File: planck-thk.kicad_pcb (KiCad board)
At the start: 2 copper layers, 228 x 114 mm, 134 parts, among them J2 Conn_01x05, J3 Qwiic, J4 Qwiic, J5 Qwiic, J6 JTAG, J7 ISP, J8 Reset, K1 Switch, K10 Switch, K11 Switch, K12 Switch, K13 Switch, K14 Switch, K15 Switch, K16 Switch, K17 Switch, K18 Switch, K19 Switch, K2 Switch, K20 Switch, K21 Switch, K22 Switch, K23 Switch, K24 Switch, K25 Switch, K26 Switch, K27 Switch, K28 Switch, K29 Switch, K3 Switch, K30 Switch, K31 Switch, K32 Switch, K33 Switch, K34 Switch, K35 Switch, K36 Switch, K37 Switch, K38 Switch, K39 Switch, K4 Switch, K40 Switch, K41 Switch, K42 Switch, K43 Switch, K44 Switch, K45 Switch, K46 Switch, K47 Switch, K48 Switch, K49 Switch, K5 Switch, K6 Switch, K7 Switch, K8 Switch, K9 Switch, SW1 SW_DIP_x04, SW2 Rotary_Encoder, SW3 Rotary_Encoder, U1 ATMEGA32A-PU, U2 LD1117S33TR_SOT223, Y1 Crystal

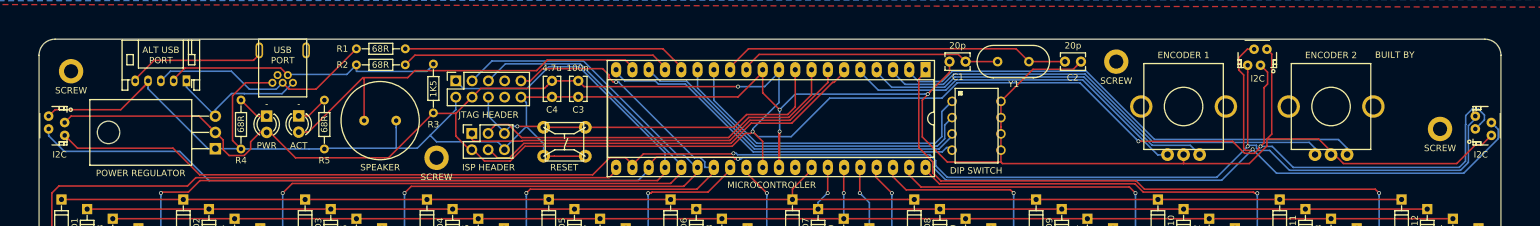
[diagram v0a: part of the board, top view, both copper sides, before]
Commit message: fix isp and jtag, usb port, remove gerbers
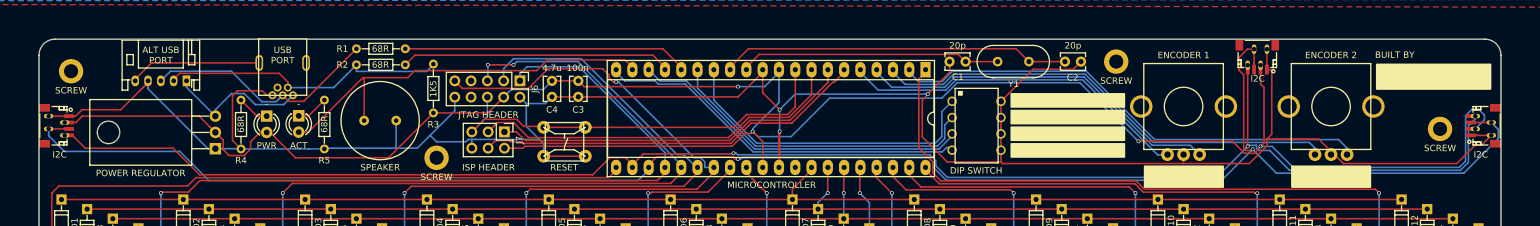
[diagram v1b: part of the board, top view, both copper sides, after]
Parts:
- J3, J4, J5: footprint olkb:JST_SZ-4 -> olkb:JST_SH_SM04B-SRSS-TB_04x1.00mm_Angled-SZ-combined
- J6: footprint Socket_Strips:Socket_Strip_Straight_2x05_Pitch2.54mm -> Pin_Headers:Pin_Header_Straight_2x05_Pitch2.54mm
- J7: footprint Socket_Strips:Socket_Strip_Straight_2x03_Pitch2.54mm -> Pin_Headers:Pin_Header_Straight_2x03_Pitch2.54mm
- moved J6 10.0 mm to (109.5, 42.0), turned to 270 degrees
- moved J7 5.09 mm to (107.1, 50.0), turned to 270 degrees
- moved USB1 1.95 mm to (72.5, 39.2)
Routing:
- net VCC: track 345.9 -> 331.5 mm
- net COL4: track 163.4 -> 174.7 mm
- net COL1: track 216.6 -> 206.3 mm
- net SDA: track 261.9 -> 271.4 mm
- net RESET: track 59.6 -> 65.5 mm, vias 1 -> 0
- net MISO: track 62.5 -> 56.7 mm
- net GND: track 368.2 -> 373.7 mm
- net COL3: track 184.6 -> 181.1 mm
- net COL2: track 196.2 -> 198.0 mm, vias 1 -> 3
- net D+: track 35.7 -> 37.3 mm
- net D-: track 44.8 -> 46.3 mm
- net SHL: track 21.8 -> 20.7 mm
- net MOSI: track 62.1 -> 61.3 mm
- net +5V: track 22.2 -> 22.9 mm

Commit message: update readme, holes sizes
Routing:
- net D+: track 37.3 -> 38.5 mm
- net D6: track 57.9 -> 58.9 mm
- net +5V: track 22.9 -> 23.5 mm
